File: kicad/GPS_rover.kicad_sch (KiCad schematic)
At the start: 17 parts, among them J401 SMA, U401 ZED_F9R

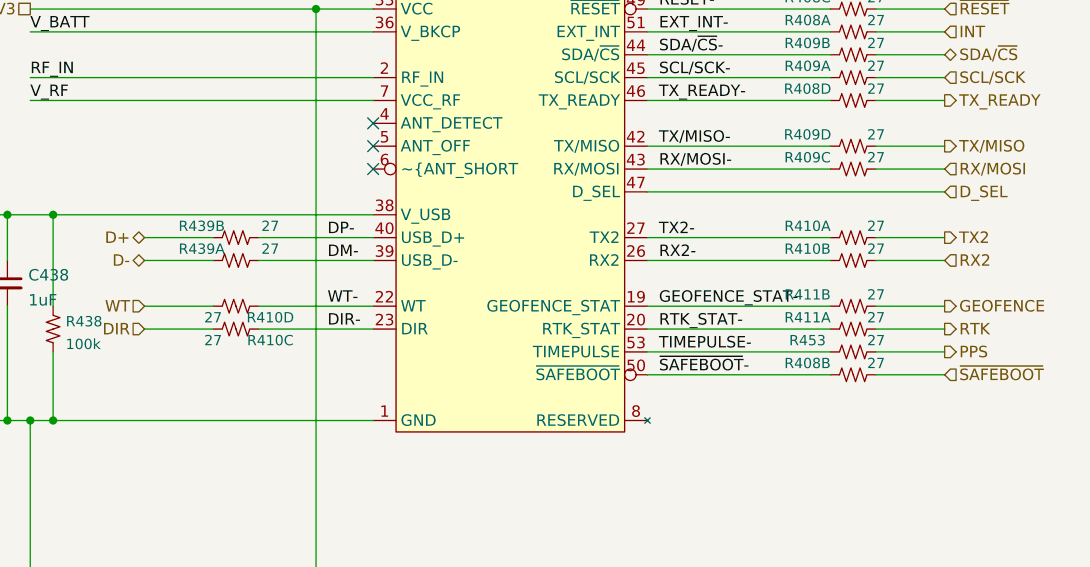
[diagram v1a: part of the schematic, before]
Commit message: One shining moment
Commit board while it still works
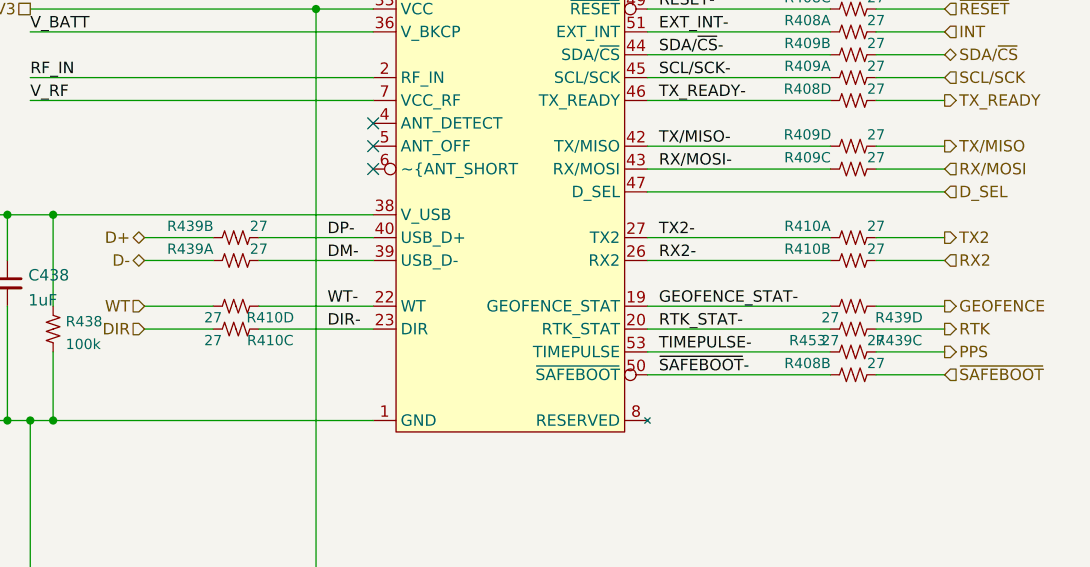
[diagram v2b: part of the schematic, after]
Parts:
- removed unit 2 of R411
- removed R439: 27, KwanSystems:R_Array_Convex_2x0402, symbol KwanSystems:RP2
- added unit 3 of R439
- added unit 4 of R439
- added unit 2 of R439
- C401: Digikey (none) -> 399-C0402C470J5GAC7867CT-ND; Purpose (none) -> Active antenna power supply
- C436, C438: Digikey (none) -> 399-C0402C105K9PAC7800CT-ND
- J401: Digikey (none) -> CONSMA003.062-ND
- L401: Digikey (none) -> 445-180949-1-ND; Purpose (none) -> Active antenna power supply
- R407: Purpose (none) -> Active antenna power supply
- R439: renamed from R411; footprint KwanSystems:R_Array_Convex_2x0402 -> KwanSystems:R_Array_Convex_4x0402; symbol KwanSystems:RP2 -> KwanSystems:RP4
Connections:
- net D+: now also R439.2 (4)
- net D-: now also R439.1 (4)
- net DM-: now also R439.8 (5)
- net DP-: now also R439.7 (5)
- net GEOFENCE: now also R439.4
- net GEOFENCE_STAT-: now also R439.5
- net RTK: now also R439.3 (4); no longer R439.4 (3)
- net RTK_STAT-: now also R439.6 (5); no longer R439.1 (4)
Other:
- moved on the sheet: R439A
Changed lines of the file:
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@@
       (effects (font (size 1.27 1.27)) hide)
     )
-    (property "Datasheet" "https://product.tdk.com/info/en/catalog/datasheets/mlcc_commercial_general_en.pdf" (id 3) (at 120.65 170.18 0)
-      (effects (font (size 1.27 1.27)) hide)
-    )
-    (property "Digikey" "" (id 4) (at 120.65 170.18 0)
+    (property "Datasheet" "~" (id 3) (at 120.65 170.18 0)
+      (effects (font (size 1.27 1.27)) hide)
+    )
+    (property "Digikey" "399-C0402C105K9PAC7800CT-ND" (id 4) (at 120.65 170.18 0)
       (effects (font (size 1.27 1.27)) hide)
     )
@@
     (pin "1")
     (pin "8")
-  )
-  (symbol (lib_id "KwanSystems:RP2") (at 167.64 83.82 0) (unit 2)
-    (in_bom yes) (on_board yes)
-    (property "Reference" "R411" (id 0) (at 162.56 82.55 0)
-      (effects (font (size 1.143 1.143)))
-    )
-    (property "Value" "27" (id 1) (at 170.18 82.55 0)
-      (effects (font (size 1.143 1.143)))
-    )
-    (property "Footprint" "KwanSystems:R_Array_Convex_2x0402" (id 2) (at 169.037 80.01 0)
-      (effects (font (size 0.508 0.508)) hide)
-    )
-    (property "Datasheet" "" (id 3) (at 178.435 91.44 0)
-      (effects (font (size 1.524 1.524)) hide)
-    )
-    (pin "2")
-    (pin "3")
   )
   (symbol (lib_id "KwanSystems:RP4") (at 167.64 53.34 0) (unit 1)
@@
       (effects (font (size 1.27 1.27)) hide)
     )
-    (pin "1")
-    (pin "2")
+    (property "Purpose" "Active antenna power supply" (id 4) (at 156.21 154.94 0)
+      (effects (font (size 1.27 1.27)) hide)
+    )
+    (property "Digikey" "445-180949-1-ND" (id 5) (at 156.21 154.94 0)
+      (effects (font (size 1.27 1.27)) hide)
+    )
+    (pin "1")
+    (pin "2")
+  )
+  (symbol (lib_id "KwanSystems:RP4") (at 167.64 86.36 180) (unit 3)
+    (in_bom yes) (on_board yes)
+    (property "Reference" "R439" (id 0) (at 172.72 87.63 0)
+      (effects (font (size 1.143 1.143)))
+    )
+    (property "Value" "27" (id 1) (at 165.1 87.63 0)
+      (effects (font (size 1.143 1.143)))
+    )
+    (property "Footprint" "KwanSystems:R_Array_Convex_4x0402" (id 2) (at 166.243 90.17 0)
+      (effects (font (size 0.508 0.508)) hide)
+    )
+    (property "Datasheet" "" (id 3) (at 156.845 78.74 0)
+      (effects (font (size 1.524 1.524)) hide)
+    )
+    (pin "3")
+    (pin "6")
+  )
+  (symbol (lib_id "KwanSystems:RP4") (at 167.64 83.82 180) (unit 4)
+    (in_bom yes) (on_board yes)
+    (property "Reference" "R439" (id 0) (at 172.72 85.09 0)
+      (effects (font (size 1.143 1.143)))
+    )
+    (property "Value" "27" (id 1) (at 165.1 85.09 0)
+      (effects (font (size 1.143 1.143)))
+    )
+    (property "Footprint" "KwanSystems:R_Array_Convex_4x0402" (id 2) (at 166.243 87.63 0)
+      (effects (font (size 0.508 0.508)) hide)
+    )
+    (property "Datasheet" "" (id 3) (at 156.845 76.2 0)
+      (effects (font (size 1.524 1.524)) hide)
+    )
+    (pin "4")
+    (pin "5")
   )
   (symbol (lib_id "KwanSystems:RP4") (at 167.64 78.74 0) (unit 2)
@@
     (pin "7")
   )
-  (symbol (lib_id "KwanSystems:RP2") (at 99.06 78.74 0) (unit 1)
-    (in_bom yes) (on_board yes)
-    (property "Reference" "R439" (id 0) (at 95.25 77.47 0)
-      (effects (font (size 1.143 1.143)))
-    )
-    (property "Value" "27" (id 1) (at 102.87 77.47 0)
-      (effects (font (size 1.143 1.143)))
-    )
-    (property "Footprint" "KwanSystems:R_Array_Convex_2x0402" (id 2) (at 100.457 74.93 0)
-      (effects (font (size 0.508 0.508)) hide)
-    )
-    (property "Datasheet" "" (id 3) (at 109.855 86.36 0)
-      (effects (font (size 1.524 1.524)) hide)
-    )
-    (property "Purpose" "USB ballast" (id 4) (at 99.06 78.74 0)
-      (effects (font (size 1.27 1.27)) hide)
-    )
-    (pin "1")
-    (pin "4")
+  (symbol (lib_id "KwanSystems:RP4") (at 99.06 76.2 0) (unit 2)
+    (in_bom yes) (on_board yes)
+    (property "Reference" "R439" (id 0) (at 93.98 74.93 0)
+      (effects (font (size 1.143 1.143)))
+    )
+    (property "Value" "27" (id 1) (at 101.6 74.93 0)
+      (effects (font (size 1.143 1.143)))
+    )
+    (property "Footprint" "KwanSystems:R_Array_Convex_4x0402" (id 2) (at 100.457 72.39 0)
+      (effects (font (size 0.508 0.508)) hide)
+    )
+    (property "Datasheet" "" (id 3) (at 109.855 83.82 0)
+      (effects (font (size 1.524 1.524)) hide)
+    )
+    (pin "2")
+    (pin "7")
   )
   (symbol (lib_id "Connector:Conn_Coaxial") (at 144.78 149.86 0) (mirror y) (unit 1)
@@
       (effects (font (size 1.27 1.27)) hide)
     )
+    (property "Digikey" "CONSMA003.062-ND" (id 5) (at 144.78 149.86 0)
+      (effects (font (size 1.27 1.27)) hide)
+    )
     (pin "1")
     (pin "2")
@@
       (effects (font (size 1.27 1.27)) hide)
     )
-    (property "Datasheet" "https://b2b-api.panasonic.eu/file_stream/pids/fileversion/1242" (id 3) (at 107.95 158.75 0)
+    (property "Datasheet" "~" (id 3) (at 107.95 158.75 0)
       (effects (font (size 1.27 1.27)) hide)
     )
@@
     (pin "2")
   )
-  (symbol (lib_id "KwanSystems:RP2") (at 167.64 86.36 0) (unit 1)
-    (in_bom yes) (on_board yes)
-    (property "Reference" "R411" (id 0) (at 162.56 85.09 0)
-      (effects (font (size 1.143 1.143)))
-    )
-    (property "Value" "27" (id 1) (at 170.18 85.09 0)
-      (effects (font (size 1.143 1.143)))
-    )
-    (property "Footprint" "KwanSystems:R_Array_Convex_2x0402" (id 2) (at 169.037 82.55 0)
-      (effects (font (size 0.508 0.508)) hide)
-    )
-    (property "Datasheet" "" (id 3) (at 178.435 93.98 0)
-      (effects (font (size 1.524 1.524)) hide)
-    )
-    (pin "1")
-    (pin "4")
+  (symbol (lib_id "KwanSystems:RP4") (at 99.06 78.74 0) (unit 1)
+    (in_bom yes) (on_board yes)
+    (property "Reference" "R439" (id 0) (at 93.98 77.47 0)
+      (effects (font (size 1.143 1.143)))
+    )
+    (property "Value" "27" (id 1) (at 101.6 77.47 0)
+      (effects (font (size 1.143 1.143)))
+    )
+    (property "Footprint" "KwanSystems:R_Array_Convex_4x0402" (id 2) (at 100.457 74.93 0)
+      (effects (font (size 0.508 0.508)) hide)
+    )
+    (property "Datasheet" "" (id 3) (at 109.855 86.36 0)
+      (effects (font (size 1.524 1.524)) hide)
+    )
+    (pin "1")
+    (pin "8")
   )
   (symbol (lib_id "Device:C_Small") (at 156.21 167.64 0) (unit 1)
@@
     )
     (property "Datasheet" "~" (id 3) (at 156.21 167.64 0)
+      (effects (font (size 1.27 1.27)) hide)
+    )
+    (property "Purpose" "Active antenna power supply" (id 4) (at 156.21 167.64 0)
+      (effects (font (size 1.27 1.27)) hide)
+    )
+    (property "Digikey" "399-C0402C470J5GAC7867CT-ND" (id 5) (at 156.21 167.64 0)
       (effects (font (size 1.27 1.27)) hide)
     )
@@
       (effects (font (size 1.524 1.524)) hide)
     )
+    (property "Purpose" "Active antenna power supply" (id 4) (at 160.02 162.56 0)
+      (effects (font (size 1.27 1.27)) hide)
+    )
     (pin "1")
     (pin "2")
@@
       (effects (font (size 1.27 1.27)) hide)
     )
+    (property "Digikey" "399-C0402C105K9PAC7800CT-ND" (id 5) (at 73.66 81.28 0)
+      (effects (font (size 1.27 1.27)) hide)
+    )
     (pin "1")
     (pin "2")
@@
       (effects (font (size 1.27 1.27)) hide)
     )
-    (property "Datasheet" "https://media.digikey.com/PDF/Data%20Sheets/Seiko%20Instruments%20PDFs/ML414H_E.pdf" (id 3) (at 107.95 171.196 90)
+    (property "Datasheet" "~" (id 3) (at 107.95 171.196 90)
       (effects (font (size 1.27 1.27)) hide)
     )
@@
     (pin "2")
   )
-  (symbol (lib_id "KwanSystems:RP2") (at 99.06 76.2 0) (unit 2)
-    (in_bom yes) (on_board yes)
-    (property "Reference" "R439" (id 0) (at 95.25 74.93 0)
-      (effects (font (size 1.143 1.143)))
-    )
-    (property "Value" "27" (id 1) (at 102.87 74.93 0)
-      (effects (font (size 1.143 1.143)))
-    )
-    (property "Footprint" "KwanSystems:R_Array_Convex_2x0402" (id 2) (at 100.457 72.39 0)
-      (effects (font (size 0.508 0.508)) hide)
-    )
-    (property "Datasheet" "" (id 3) (at 109.855 83.82 0)
-      (effects (font (size 1.524 1.524)) hide)
-    )
-    (property "Purpose" "USB ballast" (id 4) (at 99.06 76.2 0)
-      (effects (font (size 1.27 1.27)) hide)
-    )
-    (pin "2")
-    (pin "3")
-  )
   (symbol (lib_id "Device:D_Schottky_Small_Filled") (at 107.95 144.78 270) (mirror x) (unit 1)

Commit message: Updated symbol
This incorporates the change in the library, to offset the NC pins and satisfy the ERC
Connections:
- now unconnected: U401.10 (RESERVED), U401.11 (RESERVED), U401.13 (RESERVED), U401.15 (RESERVED), U401.16 (RESERVED), U401.17 (RESERVED), U401.18 (RESERVED), U401.21 (RESERVED), U401.24 (RESERVED), U401.25 (RESERVED), U401.28 (RESERVED), U401.29 (RESERVED), U401.30 (RESERVED), U401.31 (RESERVED), U401.35 (RESERVED), U401.52 (RESERVED), U401.54 (RESERVED), U401.8 (RESERVED), U401.9 (RESERVED)

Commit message: Added Digikey numbers and purposes to several parts
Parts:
- R407: Digikey (none) -> P27JCT-ND
- R408, R409, R410, R439: Digikey (none) -> 741C083270JPCT-ND; Purpose (none) -> GPS input protection
- R436: Digikey (none) -> P5.1KJCT-ND
- R438: Digikey (none) -> P100KJCT-ND
- R453: Digikey (none) -> P27JCT-ND; Purpose (none) -> GPS Timepulse protection
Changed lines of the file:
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@@
       (effects (font (size 1.524 1.524)) hide)
+    )
+    (property "Digikey" "741C083270JPCT-ND" (id 4) (at 167.64 60.96 0)
+      (effects (font (size 1.27 1.27)) hide)
+    )
+    (property "Purpose" "GPS input protection" (id 5) (at 167.64 60.96 0)
+      (effects (font (size 1.27 1.27)) hide)
     )
     (pin "4")
@@
       (effects (font (size 1.524 1.524)) hide)
     )
+    (property "Digikey" "741C083270JPCT-ND" (id 4) (at 99.06 86.36 0)
+      (effects (font (size 1.27 1.27)) hide)
+    )
+    (property "Purpose" "GPS input protection" (id 5) (at 99.06 86.36 0)
+      (effects (font (size 1.27 1.27)) hide)
+    )
     (pin "3")
     (pin "6")
@@
       (effects (font (size 1.524 1.524)) hide)
     )
+    (property "Digikey" "741C083270JPCT-ND" (id 4) (at 167.64 76.2 0)
+      (effects (font (size 1.27 1.27)) hide)
+    )
+    (property "Purpose" "GPS input protection" (id 5) (at 167.64 76.2 0)
+      (effects (font (size 1.27 1.27)) hide)
+    )
     (pin "1")
     (pin "8")
@@
       (effects (font (size 1.524 1.524)) hide)
     )
+    (property "Digikey" "741C083270JPCT-ND" (id 4) (at 167.64 53.34 0)
+      (effects (font (size 1.27 1.27)) hide)
+    )
+    (property "Purpose" "GPS input protection" (id 5) (at 167.64 53.34 0)
+      (effects (font (size 1.27 1.27)) hide)
+    )
     (pin "1")
     (pin "8")
@@
     (property "Datasheet" "" (id 3) (at 178.435 73.66 0)
       (effects (font (size 1.524 1.524)) hide)
+    )
+    (property "Digikey" "741C083270JPCT-ND" (id 4) (at 167.64 66.04 0)
+      (effects (font (size 1.27 1.27)) hide)
+    )
+    (property "Purpose" "GPS input protection" (id 5) (at 167.64 66.04 0)
+      (effects (font (size 1.27 1.27)) hide)
     )
     (pin "4")
@@
       (effects (font (size 1.524 1.524)) hide)
     )
+    (property "Digikey" "741C083270JPCT-ND" (id 4) (at 167.64 86.36 0)
+      (effects (font (size 1.27 1.27)) hide)
+    )
+    (property "Purpose" "GPS input protection" (id 5) (at 167.64 86.36 0)
+      (effects (font (size 1.27 1.27)) hide)
+    )
     (pin "3")
     (pin "6")
@@
       (effects (font (size 1.524 1.524)) hide)
     )
+    (property "Digikey" "741C083270JPCT-ND" (id 4) (at 167.64 83.82 0)
+      (effects (font (size 1.27 1.27)) hide)
+    )
+    (property "Purpose" "GPS input protection" (id 5) (at 167.64 83.82 0)
+      (effects (font (size 1.27 1.27)) hide)
+    )
     (pin "4")
     (pin "5")
@@
       (effects (font (size 1.524 1.524)) hide)
     )
+    (property "Digikey" "741C083270JPCT-ND" (id 4) (at 167.64 78.74 0)
+      (effects (font (size 1.27 1.27)) hide)
+    )
+    (property "Purpose" "GPS input protection" (id 5) (at 167.64 78.74 0)
+      (effects (font (size 1.27 1.27)) hide)
+    )
     (pin "2")
     (pin "7")
@@
     (property "Datasheet" "" (id 3) (at 109.855 83.82 0)
       (effects (font (size 1.524 1.524)) hide)
+    )
+    (property "Digikey" "741C083270JPCT-ND" (id 4) (at 99.06 76.2 0)
+      (effects (font (size 1.27 1.27)) hide)
+    )
+    (property "Purpose" "GPS input protection" (id 5) (at 99.06 76.2 0)
+      (effects (font (size 1.27 1.27)) hide)
     )
     (pin "2")
@@
       (effects (font (size 1.27 1.27)) hide)
     )
-    (property "Digikey" "" (id 4) (at 107.95 158.75 0)
+    (property "Digikey" "P5.1KJCT-ND" (id 4) (at 107.95 158.75 0)
       (effects (font (size 1.27 1.27)) hide)
     )
@@
     (property "Datasheet" "" (id 3) (at 109.855 86.36 0)
       (effects (font (size 1.524 1.524)) hide)
+    )
+    (property "Digikey" "741C083270JPCT-ND" (id 4) (at 99.06 78.74 0)
+      (effects (font (size 1.27 1.27)) hide)
+    )
+    (property "Purpose" "GPS input protection" (id 5) (at 99.06 78.74 0)
+      (effects (font (size 1.27 1.27)) hide)
     )
     (pin "1")
@@
       (effects (font (size 1.524 1.524)) hide)
     )
+    (property "Digikey" "741C083270JPCT-ND" (id 4) (at 167.64 55.88 0)
+      (effects (font (size 1.27 1.27)) hide)
+    )
+    (property "Purpose" "GPS input protection" (id 5) (at 167.64 55.88 0)
+      (effects (font (size 1.27 1.27)) hide)
+    )
     (pin "2")
     (pin "7")
@@
       (effects (font (size 1.524 1.524)) hide)
     )
+    (property "Digikey" "741C083270JPCT-ND" (id 4) (at 167.64 58.42 0)
+      (effects (font (size 1.27 1.27)) hide)
+    )
+    (property "Purpose" "GPS input protection" (id 5) (at 167.64 58.42 0)
+      (effects (font (size 1.27 1.27)) hide)
+    )
     (pin "1")
     (pin "8")
@@
     (property "Datasheet" "" (id 3) (at 88.265 76.2 0)
       (effects (font (size 1.524 1.524)) hide)
+    )
+    (property "Digikey" "741C083270JPCT-ND" (id 4) (at 99.06 83.82 0)
+      (effects (font (size 1.27 1.27)) hide)
+    )
+    (property "Purpose" "GPS input protection" (id 5) (at 99.06 83.82 0)
+      (effects (font (size 1.27 1.27)) hide)
     )
     (pin "4")
@@
       (effects (font (size 1.27 1.27)) hide)
     )
+    (property "Digikey" "P27JCT-ND" (id 5) (at 160.02 162.56 0)
+      (effects (font (size 1.27 1.27)) hide)
+    )
     (pin "1")
     (pin "2")
@@
       (effects (font (size 1.524 1.524)) hide)
     )
+    (property "Digikey" "P27JCT-ND" (id 4) (at 167.64 88.9 0)
+      (effects (font (size 1.27 1.27)) hide)
+    )
+    (property "Purpose" "GPS Timepulse protection" (id 5) (at 167.64 88.9 0)
+      (effects (font (size 1.27 1.27)) hide)
+    )
     (pin "1")
     (pin "2")
@@
     (property "Datasheet" "" (id 3) (at 178.435 58.42 0)
       (effects (font (size 1.524 1.524)) hide)
+    )
+    (property "Digikey" "741C083270JPCT-ND" (id 4) (at 167.64 50.8 0)
+      (effects (font (size 1.27 1.27)) hide)
+    )
+    (property "Purpose" "GPS input protection" (id 5) (at 167.64 50.8 0)
+      (effects (font (size 1.27 1.27)) hide)
     )
     (pin "3")
@@
       (effects (font (size 1.524 1.524)) hide)
     )
+    (property "Digikey" "741C083270JPCT-ND" (id 4) (at 167.64 91.44 0)
+      (effects (font (size 1.27 1.27)) hide)
+    )
+    (property "Purpose" "GPS input protection" (id 5) (at 167.64 91.44 0)
+      (effects (font (size 1.27 1.27)) hide)
+    )
     (pin "2")
     (pin "7")
@@
     (property "Datasheet" "" (id 3) (at 178.435 76.2 0)
       (effects (font (size 1.524 1.524)) hide)
+    )
+    (property "Digikey" "741C083270JPCT-ND" (id 4) (at 167.64 68.58 0)
+      (effects (font (size 1.27 1.27)) hide)
+    )
+    (property "Purpose" "GPS input protection" (id 5) (at 167.64 68.58 0)
+      (effects (font (size 1.27 1.27)) hide)
     )
     (pin "3")
@@
       (effects (font (size 1.27 1.27)) hide)
     )
+    (property "Digikey" "P100KJCT-ND" (id 5) (at 78.74 86.36 0)
+      (effects (font (size 1.27 1.27)) hide)
+    )

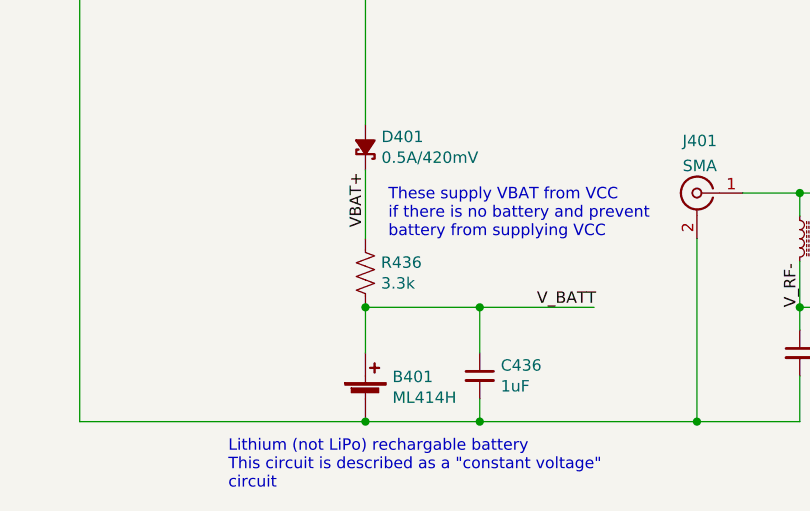
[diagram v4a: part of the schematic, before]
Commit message: Changed value of R436
This is the current limiter for the battery charging. It slows down the charging, in exchange for reducing the number of different components
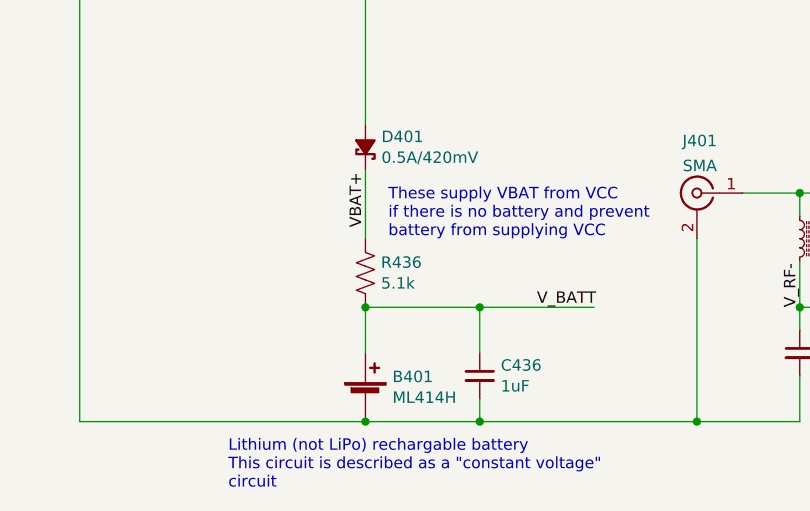
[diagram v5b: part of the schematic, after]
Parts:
- R436: value 3.3k -> 5.1k
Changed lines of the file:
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@@
       (effects (font (size 1.27 1.27)) (justify left))
     )
-    (property "Value" "3.3k" (id 1) (at 109.6772 159.893 0)
+    (property "Value" "5.1k" (id 1) (at 109.6772 159.893 0)
       (effects (font (size 1.27 1.27)) (justify left))
     )
